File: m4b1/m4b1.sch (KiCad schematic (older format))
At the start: 33 parts, among them U1 MC306, U10 MC308, U11 MC306, U12 MC311, U14 MC306, U15 MC308, U16 MC306, U17 MC311, U19 MC308, U2 MC310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

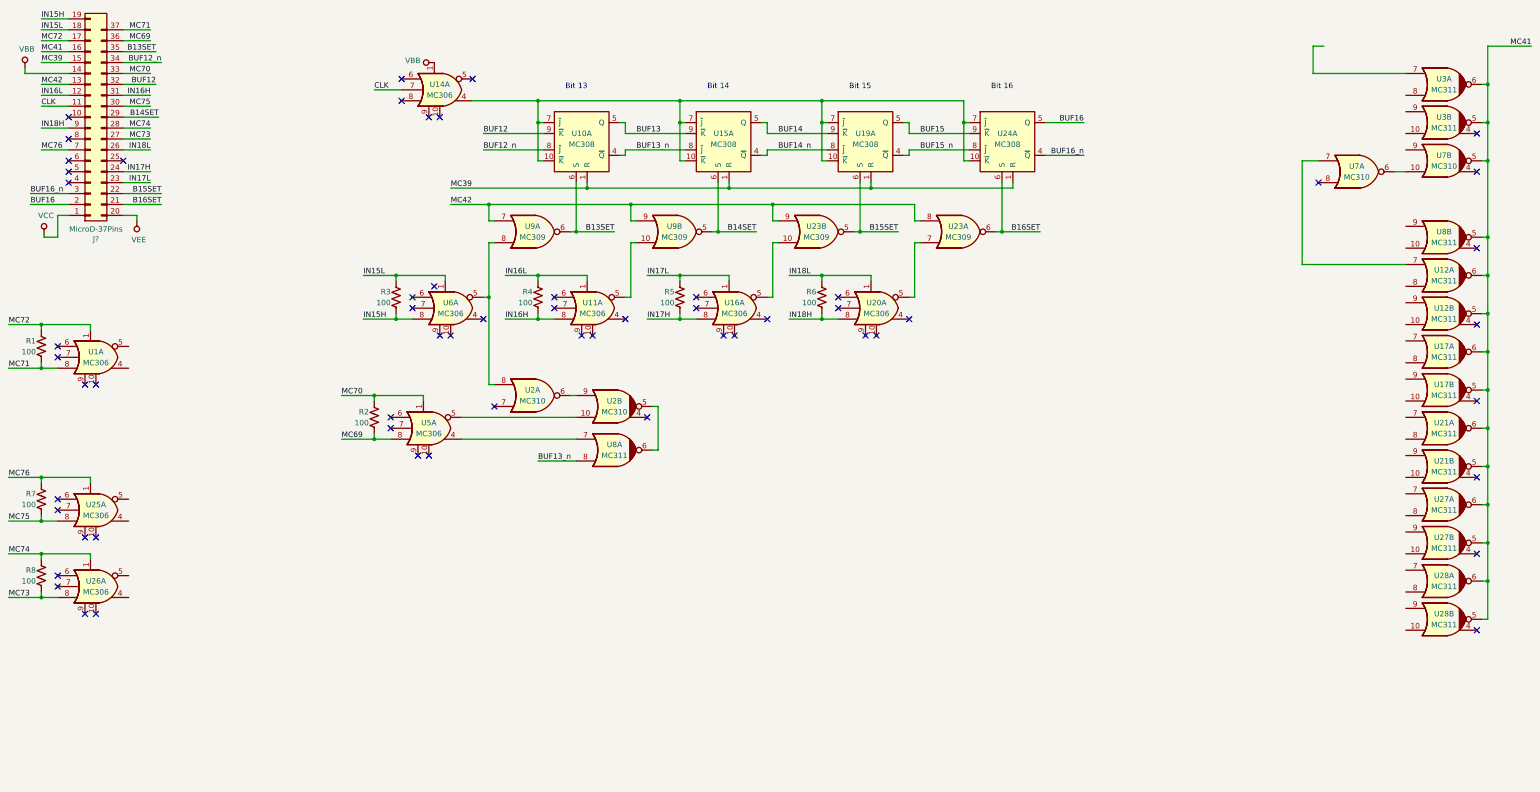
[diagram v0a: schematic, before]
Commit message: Completed schematic for module 4, board 1.
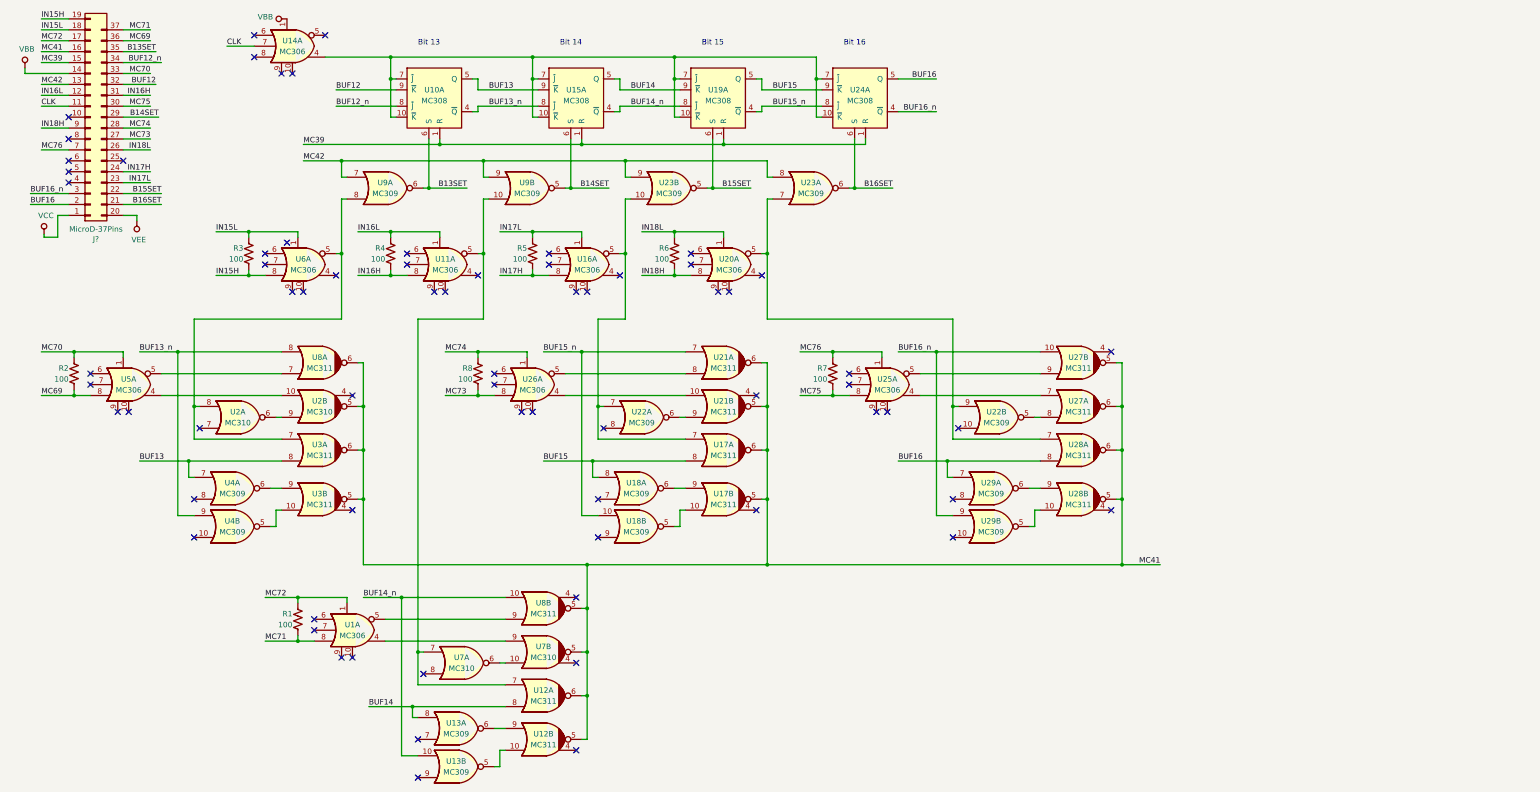
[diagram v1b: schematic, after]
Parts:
- added U13, U18, U22, U29, U4: MC309, symbol gn_buffer:MC309
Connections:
- net BUF13: now also U3.8, U4.7
- net BUF13_n: now also U4.9
- net BUF14: now also U12.8, U13.8
- net BUF14_n: now also U8.10, U13.10
- net BUF15: now also U17.8, U18.8
- net BUF15_n: now also U21.7, U18.10
- net BUF16: now also U28.8, U29.7
- net BUF16_n: now also U27.10, U29.9
- net MC41: now also U2.5, U8.6
- net at U1.4: now also U7.9
- net at U1.5: now also U8.9
- net at U5.4: now also U2.10; no longer U8.7
- net at U5.5: now also U8.7; no longer U2.10
- net at U2.8, U6.5, U9.8: now also U3.7
- net at U11.5, U9.10: now also U12.7, U7.7
- net at U16.5, U23.10: now also U17.7, U22.7
- net at U20.5, U23.7: now also U28.7, U22.9
- net at U25.4: now also U27.7
- net at U25.5: now also U27.9
- net at U26.4: now also U21.10
- net at U26.5: now also U21.8
- net at U3.10: now also U4.5
- net at U3.9: now also U4.6
- net at U12.10: now also U13.5
- net at U12.9: now also U13.6
- net at U17.10: now also U18.5
- net at U17.9: now also U18.6
- net at U21.9: now also U22.6
- net at U27.8: now also U22.5
- net at U28.10: now also U29.5
- net at U28.9: now also U29.6
- no-connect marks 59 -> 69
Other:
- moved on the sheet: R1, R2, R3, R4, R5, R6, R7, R8, U10A, U11A, U12A, U12B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

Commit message: Finished untangling the module 3 schematics and gave every net a name
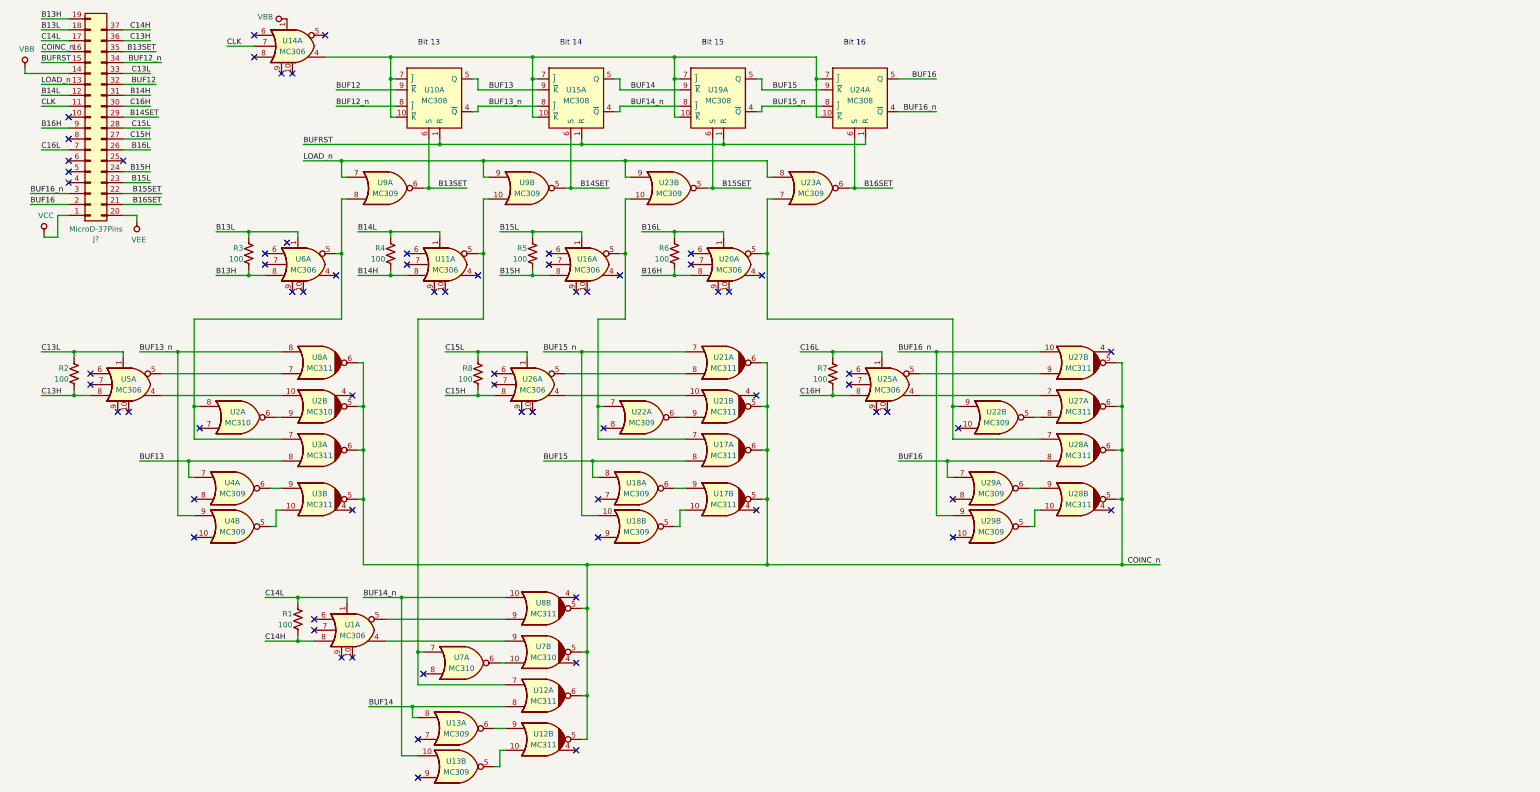
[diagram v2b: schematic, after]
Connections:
- net IN15H renamed B13H
- net IN15L renamed B13L
- net IN16H renamed B14H
- net IN16L renamed B14L
- net IN17H renamed B15H
- net IN17L renamed B15L
- net IN18H renamed B16H
- net IN18L renamed B16L
- net MC39 renamed BUFRST
- net MC41 renamed COINC_n
- net MC42 renamed LOAD_n
- net MC69 renamed C13H
- net MC70 renamed C13L
- net MC71 renamed C14H
- net MC72 renamed C14L
- net MC73 renamed C15H
- net MC74 renamed C15L
- net MC75 renamed C16H
- net MC76 renamed C16L
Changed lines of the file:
@@
 $EndComp
 Text Label 800  1850 0    50   ~ 0
-MC76
+C16L
 Wire Wire Line
 	1050 1850 800  1850
 Text Label 1800 1450 2    50   ~ 0
-MC75
+C16H
 Wire Wire Line
 	1550 1450 1800 1450
@@
 	1550 1650 1800 1650
 Text Label 1800 1750 2    50   ~ 0
-MC73
+C15H
 Wire Wire Line
 	1550 1750 1800 1750
 Text Label 800  850  0    50   ~ 0
-MC72
+C14L
 Wire Wire Line
 	1050 850  800  850
 Text Label 1800 750  2    50   ~ 0
-MC71
+C14H
 Wire Wire Line
 	1550 750  1800 750
 Text Label 1800 1150 2    50   ~ 0
-MC70
+C13L
 Wire Wire Line
 	1550 1150 1800 1150
 Text Label 1800 850  2    50   ~ 0
-MC69
+C13H
 Wire Wire Line
 	1550 850  1800 850
@@
 	1050 2350 700  2350
 Text Label 1800 1850 2    50   ~ 0
-IN18L
+B16L
 Wire Wire Line
 	1550 1850 1800 1850
 Text Label 800  1650 0    50   ~ 0
-IN18H
+B16H
 Wire Wire Line
 	1050 1650 800  1650
 Text Label 1800 2150 2    50   ~ 0
-IN17L
+B15L
 Wire Wire Line
 	1550 2150 1800 2150
 Text Label 1800 2050 2    50   ~ 0
-IN17H
+B15H
 Wire Wire Line
 	1550 2050 1800 2050
 Text Label 800  1350 0    50   ~ 0
-IN16L
+B14L
 Wire Wire Line
 	1050 1350 800  1350
 Text Label 1800 1350 2    50   ~ 0
-IN16H
+B14H
 Wire Wire Line
 	1550 1350 1800 1350
 Text Label 800  750  0    50   ~ 0
-IN15L
+B13L
 Wire Wire Line
 	1050 750  800  750
 Text Label 800  650  0    50   ~ 0
-IN15H
+B13H
 Wire Wire Line
 	1050 650  800  650
@@
 	1050 2250 700  2250
 Text Label 1800 1650 2    50   ~ 0
-MC74
+C15L
 Wire Wire Line
 	1550 1250 1850 1250
@@
 BUF12_n
 Text Label 800  950  0    50   ~ 0
-MC41
+COINC_n
 Wire Wire Line
 	1050 950  800  950
 Text Label 800  1050 0    50   ~ 0
-MC39
+BUFRST
 Wire Wire Line
 	800  1050 1050 1050
@@
 	800  1250 1050 1250
 Text Label 800  1250 0    50   ~ 0
-MC42
+LOAD_n
 Wire Wire Line
 	950  2650 950  2450
@@
 Connection ~ 3150 6350
 Text Label 2850 5950 0    50   ~ 0
-MC72
+C14L
 Text Label 2850 6350 0    50   ~ 0
-MC71
+C14H
 NoConn ~ 1500 4250
 NoConn ~ 1600 4250
@@
 Connection ~ 1100 4100
 Text Label 800  3700 0    50   ~ 0
-MC70
+C13L
 Text Label 800  4100 0    50   ~ 0
-MC69
+C13H
 NoConn ~ 3100 3150
 NoConn ~ 3200 3150
@@
 Connection ~ 2700 3000
 Text Label 2400 2600 0    50   ~ 0
-IN15L
+B13L
 Text Label 2400 3000 0    50   ~ 0
-IN15H
+B13H
 NoConn ~ 4400 3150
 NoConn ~ 4500 3150
@@
 Connection ~ 4000 3000
 Text Label 3700 2600 0    50   ~ 0
-IN16L
+B14L
 Text Label 3700 3000 0    50   ~ 0
-IN16H
+B14H
 NoConn ~ 5700 3150
 NoConn ~ 5800 3150
@@
 Connection ~ 5300 3000
 Text Label 5000 2600 0    50   ~ 0
-IN17L
+B15L
 Text Label 5000 3000 0    50   ~ 0
-IN17H
+B15H
 NoConn ~ 7000 3150
 NoConn ~ 7100 3150
@@
 Connection ~ 6600 3000
 Text Label 6300 2600 0    50   ~ 0
-IN18L
+B16L
 Text Label 6300 3000 0    50   ~ 0
-IN18H
+B16H
 NoConn ~ 8450 4250
 NoConn ~ 8550 4250
@@
 Connection ~ 8050 4100
 Text Label 7750 3700 0    50   ~ 0
-MC76
+C16L
 Text Label 7750 4100 0    50   ~ 0
-MC75
+C16H
 NoConn ~ 5200 4250
 NoConn ~ 5300 4250
@@
 Connection ~ 4800 4100
 Text Label 4500 3700 0    50   ~ 0
-MC74
+C15L
 Text Label 4500 4100 0    50   ~ 0
-MC73
+C15H
 NoConn ~ 3050 2700
 $Comp
@@
 	4450 1800 3200 1800
 Text Label 3200 1800 0    50   ~ 0
-MC39
+BUFRST
 Wire Wire Line
 	4050 1550 4000 1550
@@
 B13SET
 Text Label 3200 1950 0    50   ~ 0
-MC42
+LOAD_n
 Wire Wire Line
 	3200 1950 3550 1950
@@
 Connection ~ 10700 5650
 Text Label 11050 5650 2    50   ~ 0
-MC41
+COINC_n
 $EndSCHEMATC

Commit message: Greatly cleaned up all of the schematics so far; everything passes DRC.
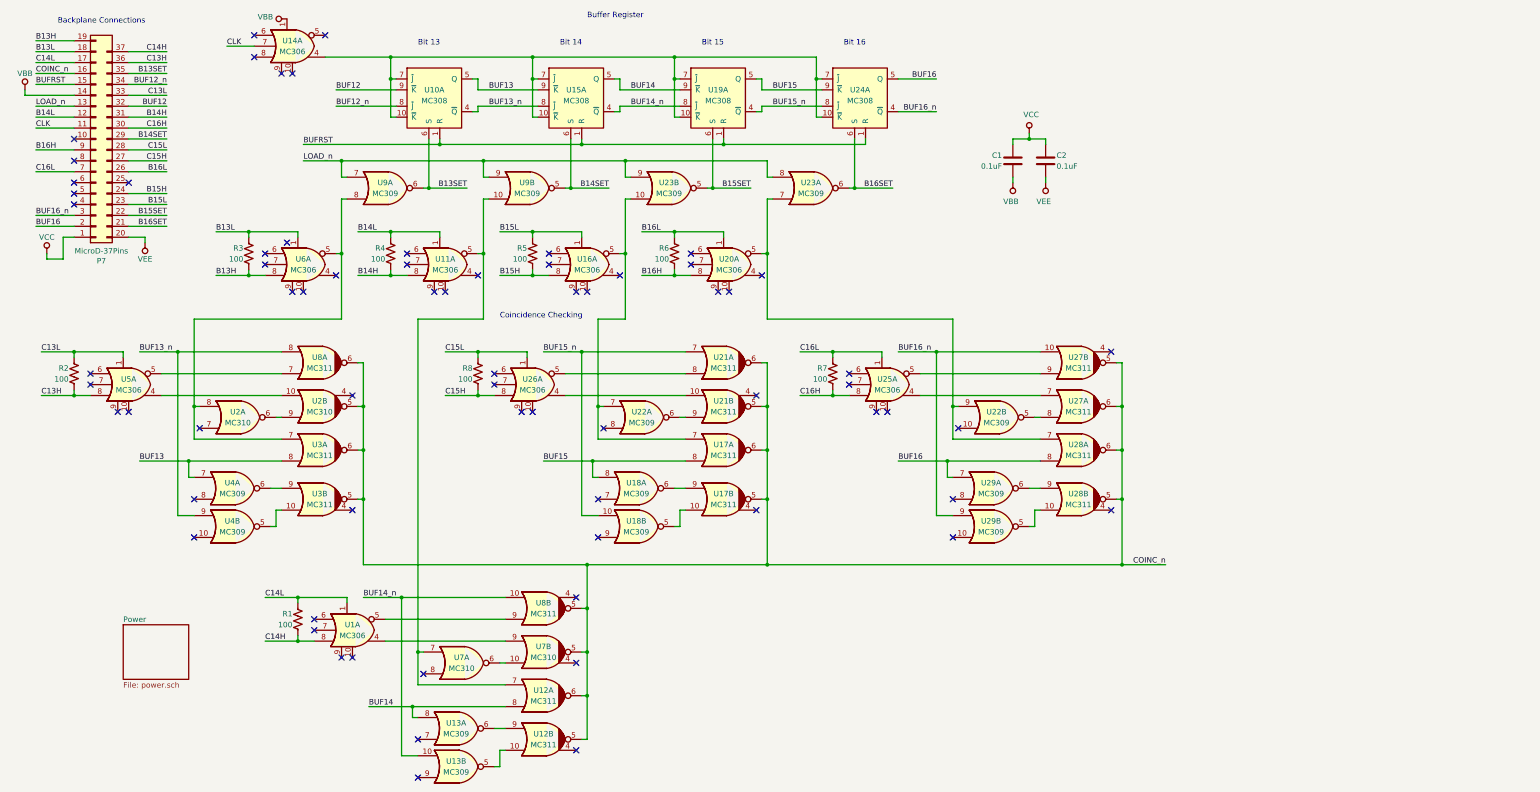
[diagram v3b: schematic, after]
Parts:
- removed J?: MicroD-37Pins, symbol gn_buffer:MicroD-37Pins
- added C1, C2: 0.1uF, symbol Device:C
- added P7: MicroD-37Pins, symbol gn_buffer:MicroD-37Pins
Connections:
- net B13H: now also P7.19 (Pin_19)
- net B13L: now also P7.18 (Pin_18)
- net B13SET: now also P7.35 (Pin_35)
- net B14H: now also P7.31 (Pin_31)
- net B14L: now also P7.12 (Pin_12)
- net B14SET: now also P7.29 (Pin_29)
- net B15H: now also P7.24 (Pin_24)
- net B15L: now also P7.23 (Pin_23)
- net B15SET: now also P7.22 (Pin_22)
- net B16H: now also P7.9 (Pin_9)
- net B16L: now also P7.26 (Pin_26)
- net B16SET: now also P7.21 (Pin_21)
- net BUF12: now also P7.32 (Pin_32)
- net BUF12_n: now also P7.34 (Pin_34)
- net BUF16: now also P7.2 (Pin_2)
- net BUF16_n: now also P7.3 (Pin_3)
- net BUFRST: now also P7.15 (Pin_15)
- net C13H: now also P7.36 (Pin_36)
- net C13L: now also P7.33 (Pin_33)
- net C14H: now also P7.37 (Pin_37)
- net C14L: now also P7.17 (Pin_17)
- net C15H: now also P7.27 (Pin_27)
- net C15L: now also P7.28 (Pin_28)
- net C16H: now also P7.30 (Pin_30)
- net C16L: now also P7.7 (Pin_7)
- net CLK: now also P7.11 (Pin_11)
- net COINC_n: now also P7.16 (Pin_16)
- net LOAD_n: now also P7.13 (Pin_13)
- net VBB: now also C1.2, P7.14 (Pin_14)
- net VCC: now also C1.1, C2.1, P7.1 (Pin_1)
- net VEE: now also C2.2, P7.20 (Pin_20)
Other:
- note added: "Backplane Connections"
- note added: "Buffer Register"
- note added: "Coincidence Checking"
